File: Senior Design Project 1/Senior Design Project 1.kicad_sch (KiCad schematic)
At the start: 20 parts, among them U1 74LS05, U2 74HC273, U3 74HC74N_652, U4 74HC74N_652, U6 LM555xN, U7 74HC08N, U9 74HC273

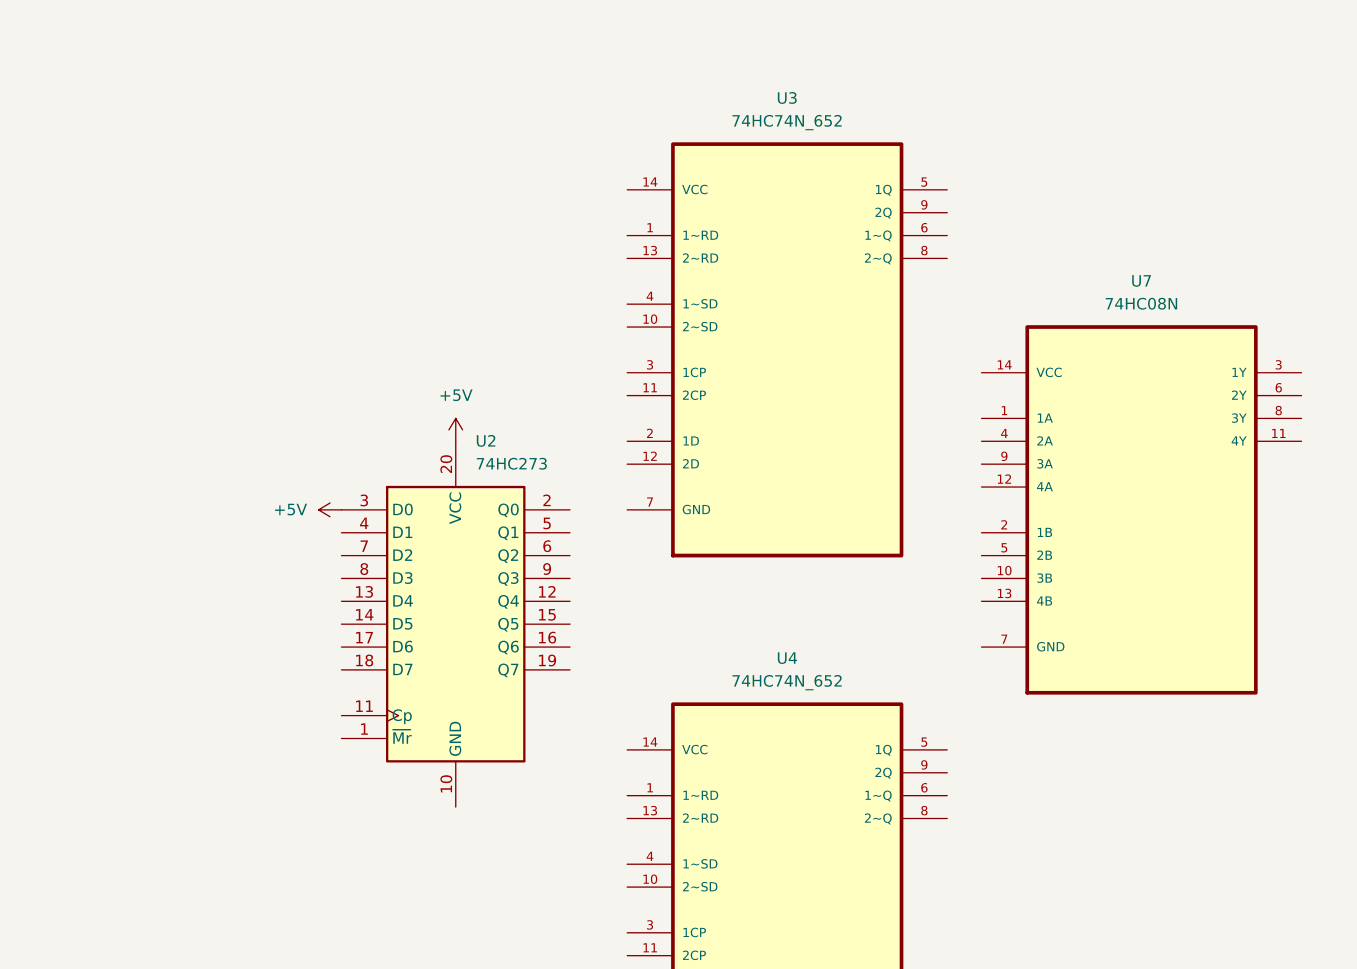
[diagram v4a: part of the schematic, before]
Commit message: Added comparator library
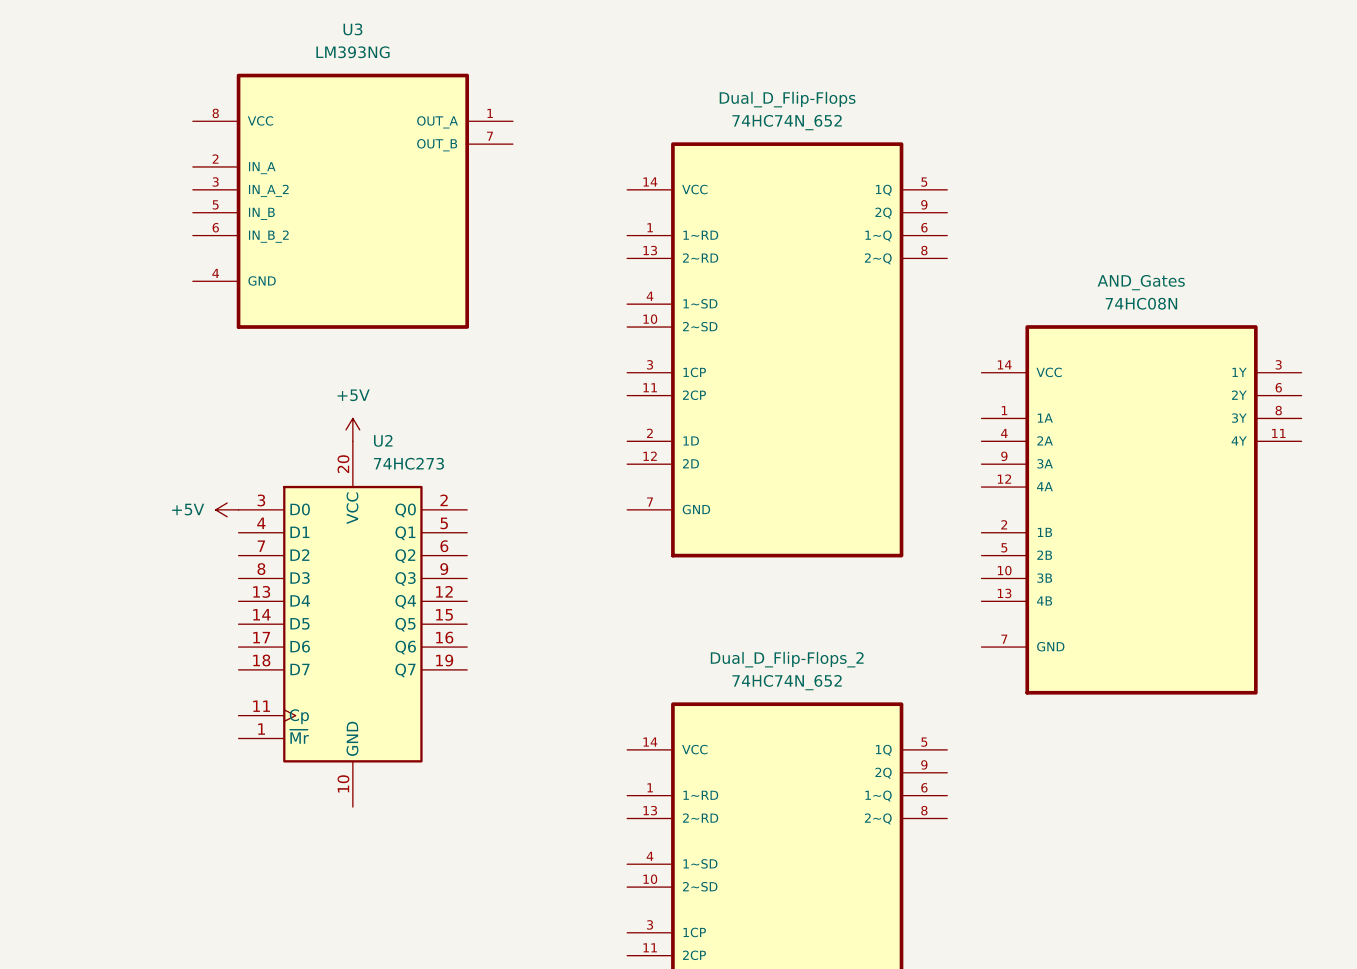
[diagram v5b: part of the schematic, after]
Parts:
- added U3: LM393NG, LM393NG:DIP254P762X533-8, symbol LM393NG:LM393NG
- renumbered U7 to AND_Gates, U3 to Dual_D_Flip-Flops, U4 to Dual_D_Flip-Flops_2
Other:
- moved on the sheet: U2

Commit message: Schematic Done for PCB Build
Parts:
- removed R17: 5.1k, Resistor_THT:R_Axial_DIN0204_L3.6mm_D1.6mm_P7.62mm_Horizontal, symbol Device:R
- added C1: 100n, Capacitor_THT:CP_Radial_D6.3mm_P2.50mm, symbol Device:C
- added C2: 10n, Capacitor_THT:CP_Radial_D6.3mm_P2.50mm, symbol Device:C
- added D1, D2, D3, D4: LED, symbol Device:LED
- added R14, R15: 510, Resistor_THT:R_Axial_DIN0204_L3.6mm_D1.6mm_P7.62mm_Horizontal, symbol Device:R
- added R2: 2.4k, Resistor_THT:R_Axial_DIN0204_L3.6mm_D1.6mm_P7.62mm_Horizontal, symbol Device:R
- R1: value 510 -> 1.2k
- R10, R11, R6, R8: value 5.1k -> 3.3k
- R12, R13: value 5.1k -> 510
- R4, R5, R7, R9: value 5.1k -> 6.6k
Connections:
- net +5V: now also AND_Gates.14 (VCC), Dual_D_Flip-Flops.14 (VCC), Dual_D_Flip-Flops_2.14 (VCC), U3.8 (VCC); no longer U2.3 (D0)
- net VDD: now reaches Dual_D_Flip-Flops_2.1 (1~RD)
- net VDD: now also AND_Gates.1 (1A), Dual_D_Flip-Flops.1 (1~RD), Dual_D_Flip-Flops.13 (2~RD), Dual_D_Flip-Flops_2.13 (2~RD), R1.1, R3.2, U2.3 (D0), U6.4 (R), U6.8 (VCC)
- net at Dual_D_Flip-Flops_2.10 (2~SD): now also Dual_D_Flip-Flops.10 (2~SD), Dual_D_Flip-Flops.4 (1~SD), Dual_D_Flip-Flops_2.4 (1~SD), U1.2, U2.1 (~{Mr})
- net at Dual_D_Flip-Flops_2.11 (2CP): now also U2.9 (Q3)
- net at Dual_D_Flip-Flops_2.12 (2D): now also Dual_D_Flip-Flops.12 (2D), Dual_D_Flip-Flops.2 (1D), Dual_D_Flip-Flops_2.2 (1D), R3.1, U3.1 (OUT_A)
- net at Dual_D_Flip-Flops_2.3 (1CP): now also AND_Gates.12 (4A), U2.6 (Q2)
- net at Dual_D_Flip-Flops_2.5 (1Q): now also AND_Gates.10 (3B)
- net GND: now reaches Dual_D_Flip-Flops_2.7 (GND)
- net GND: now also AND_Gates.7 (GND), Dual_D_Flip-Flops.7 (GND), R11.1, R12.2, R13.2, U2.10 (GND), U3.4 (GND), U6.1 (GND), U9.10 (GND), C1.2, C2.2, R14.2, R15.2
- net at Dual_D_Flip-Flops_2.9 (2Q): now also AND_Gates.13 (4B)
- net at R11.2: now also R8.1, R9.2
- net at AND_Gates.11 (4Y): now also R9.1, U9.3 (D0)
- net at AND_Gates.2 (1B): now also Dual_D_Flip-Flops.5 (1Q)
- net at AND_Gates.3 (1Y): now also R4.1, U9.8 (D3)
- net at AND_Gates.4 (2A): now also Dual_D_Flip-Flops.3 (1CP), U2.2 (Q0)
- net at AND_Gates.5 (2B): now also Dual_D_Flip-Flops.9 (2Q)
- net at AND_Gates.6 (2Y): now also R5.1, U9.7 (D2)
- net at AND_Gates.8 (3Y): now also R7.1, U9.4 (D1)
- net at AND_Gates.9 (3A): now also Dual_D_Flip-Flops.11 (2CP), U2.5 (Q1)
- net at R7.2: now also R6.1, R8.2; no longer R8.1
- net at R13.1: now also D2.1 (K)
- net at R5.2: now also R10.1, R6.2; no longer R6.1
- net +3V: now reaches U3.2 (IN_A)
- net at U3.3 (IN_A_2): now also R10.2, R4.2
- net at U1.1: now also U2.12 (Q4), U9.11 (Cp)
- net at U9.2 (Q0): now also D1.2 (A)
- net at U9.5 (Q1): now also D2.2 (A)
- net at U9.6 (Q2): now also D3.2 (A)
- net at U9.9 (Q3): now also D4.2 (A)
- net at U2.11 (Cp): now also U6.3 (Q)
- net at R12.1: now also D1.1 (K)
- net at R1.2: now also U6.7 (DIS), R2.1
- net at U6.2 (TR): now also U6.6 (THR), C1.1, R2.2
- net at U6.5 (CV): now also C2.1
- new net: D4.1 (K), R15.1
- new net: D3.1 (K), R14.1
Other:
- moved on the sheet: AND_Gates, Dual_D_Flip-Flops, Dual_D_Flip-Flops_2, R1, R10, R3, R4, U1A, U3, U6, U9

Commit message: Saves
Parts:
- D1, D2, D3, D4: footprint (none) -> LED_THT:LED_D3.0mm_Horizontal_O6.35mm_Z10.0mm
- U1: footprint (none) -> RF_Mini-Circuits:Mini-Circuits_BK377
- renumbered AND_Gates to AND_Gates1, Dual_D_Flip-Flops to Dual_D_Flip-Flops1
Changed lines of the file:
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@@
 		(dnp no)
 		(fields_autoplaced yes)
-		(property "Reference" "AND_Gates"
+		(property "Reference" "AND_Gates1"
 			(at 309.88 35.56 0)
 			(effects
@@
 			(project ""
 				(path "/26f0e0d8-48b3-4b2f-ae33-e0e1c95a5120"
-					(reference "AND_Gates")
+					(reference "AND_Gates1")
 					(unit 1)
 				)
@@
 			)
 		)
-		(property "Footprint" ""
+		(property "Footprint" "LED_THT:LED_D3.0mm_Horizontal_O6.35mm_Z10.0mm"
 			(at 414.02 129.54 0)
 			(effects
@@
 		(dnp no)
 		(fields_autoplaced yes)
-		(property "Reference" "Dual_D_Flip-Flops"
+		(property "Reference" "Dual_D_Flip-Flops1"
 			(at 243.84 35.56 0)
 			(effects
@@
 			(project ""
 				(path "/26f0e0d8-48b3-4b2f-ae33-e0e1c95a5120"
-					(reference "Dual_D_Flip-Flops")
+					(reference "Dual_D_Flip-Flops1")
 					(unit 1)
 				)
@@
 			)
 		)
-		(property "Footprint" ""
+		(property "Footprint" "LED_THT:LED_D3.0mm_Horizontal_O6.35mm_Z10.0mm"
 			(at 392.43 129.54 0)
 			(effects
@@
 			)
 		)
-		(property "Footprint" ""
+		(property "Footprint" "LED_THT:LED_D3.0mm_Horizontal_O6.35mm_Z10.0mm"
 			(at 422.91 129.54 0)
 			(effects
@@
 			)
 		)
-		(property "Footprint" ""
+		(property "Footprint" "RF_Mini-Circuits:Mini-Circuits_BK377"
 			(at 58.42 99.06 0)
 			(effects
@@
 			)
 		)
-		(property "Footprint" ""
+		(property "Footprint" "LED_THT:LED_D3.0mm_Horizontal_O6.35mm_Z10.0mm"
 			(at 402.59 129.54 0)
 			(effects

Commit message: Updated Schematic & PCB
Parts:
- added V1: 5V, TerminalBlock:TerminalBlock_bornier-3_P5.08mm, symbol Simulation_SPICE:VDC
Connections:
- net GND: now also V1.2
- net VDD: no longer R1.1, U2.3 (D0), U6.4 (R), U6.8 (VCC)
- net +5V: no longer names the net of AND_Gates1.14 (VCC), Dual_D_Flip-Flops1.14 (VCC), Dual_D_Flip-Flops_2.14 (VCC), U2.20 (VCC), U3.8 (VCC), U9.20 (VCC)
- net +5V: now also R1.1, U2.3 (D0), U6.4 (R), U6.8 (VCC), V1.1
